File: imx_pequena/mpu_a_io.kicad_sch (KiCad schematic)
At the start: 23 parts, among them J1 Conn_ARM_JTAG_SWD_10, U1 MCIMX6Z0DVM09AB, Y1 Crystal, Y2 Crystal

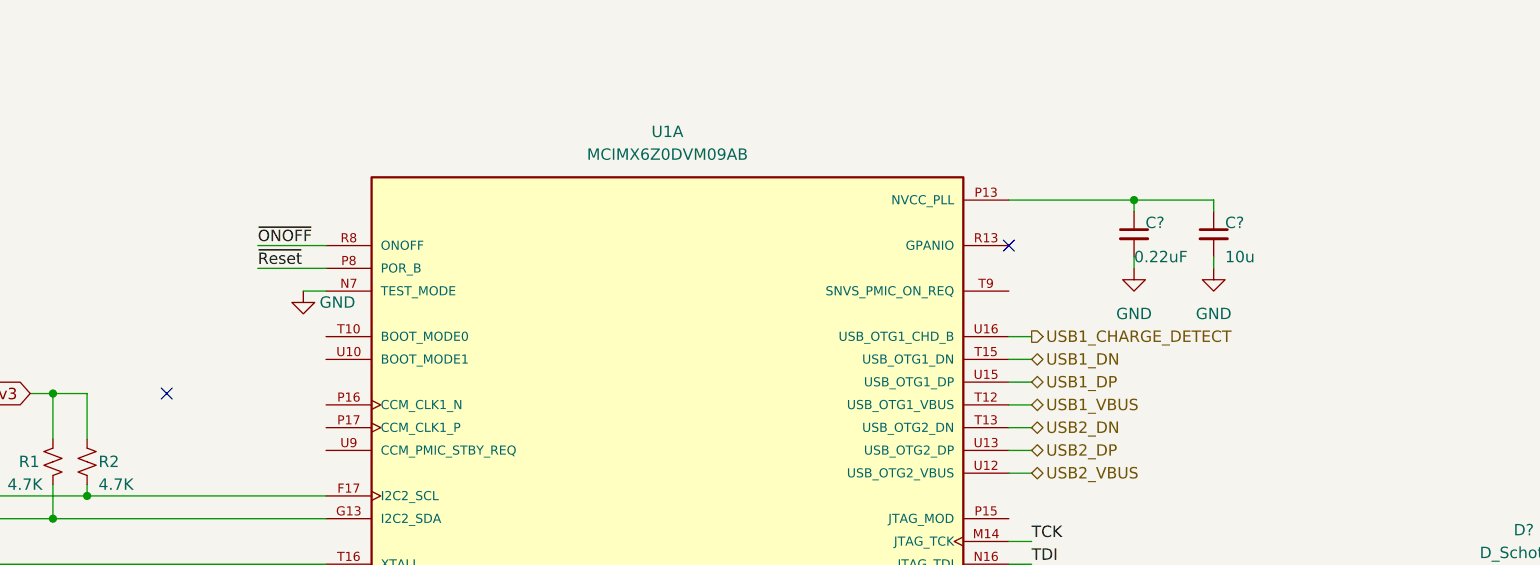
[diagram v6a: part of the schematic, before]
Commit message: Cleaned up NVCC pins
Added 3v3 connections + decoupling caps to NVcc pins
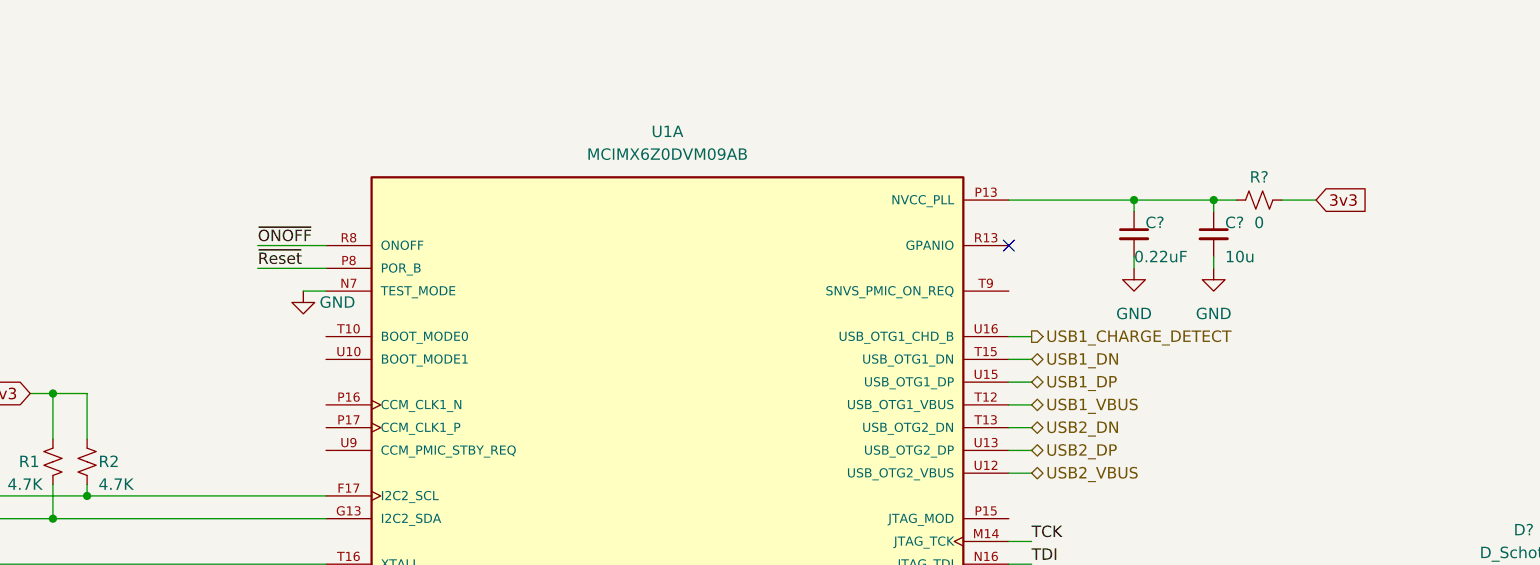
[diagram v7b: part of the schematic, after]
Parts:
- added R?: 0, symbol Device:R_Small_US
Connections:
- net at C?.1, C?.1, U1.P13 (NVCC_PLL): now also R?.1
- new net 3v3: R?.2
- no-connect marks 2 -> 1
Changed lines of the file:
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@@
   (junction (at 199.39 58.42) (diameter 0) (color 0 0 0 0)
   )
+  (junction (at 208.28 58.42) (diameter 0) (color 0 0 0 0)
+  )
   (junction (at 29.21 36.83) (diameter 0) (color 0 0 0 0)
   )
@@
   )
   (no_connect (at 185.42 63.5))
-  (no_connect (at 91.44 80.01))
   (wire (pts (xy 199.39 58.42) (xy 199.39 59.69))
     (stroke (width 0) (type default) (color 0 0 0 0))
@@
     (stroke (width 0) (type default) (color 0 0 0 0))
   )
+  (wire (pts (xy 208.28 58.42) (xy 210.82 58.42))
+    (stroke (width 0) (type default) (color 0 0 0 0))
+  )
   (wire (pts (xy 247.65 17.78) (xy 247.65 20.32))
     (stroke (width 0) (type default) (color 0 0 0 0))
@@
   )
   (wire (pts (xy 59.69 22.86) (xy 57.15 22.86))
+    (stroke (width 0) (type default) (color 0 0 0 0))
+  )
+  (wire (pts (xy 215.9 58.42) (xy 219.71 58.42))
     (stroke (width 0) (type default) (color 0 0 0 0))
   )
@@
     (property "Intersheet References" "${INTERSHEET_REFS}" (id 0) (at 45.3026 22.7806 0)
       (effects (font (size 1.27 1.27)) (justify right) hide)
+    )
+  )
+  (global_label "3v3" (shape input) (at 219.71 58.42 0) (fields_autoplaced)
+    (effects (font (size 1.27 1.27)) (justify left))
+    (property "Intersheet References" "${INTERSHEET_REFS}" (id 0) (at 225.5098 58.3406 0)
+      (effects (font (size 1.27 1.27)) (justify left) hide)
     )
   )
@@
       (effects (font (size 1.27 1.27)) hide)
     )
+    (pin "1")
+    (pin "2")
+  )
+  (symbol (lib_id "Device:R_Small_US") (at 213.36 58.42 90) (unit 1)
+    (in_bom yes) (on_board yes)
+    (property "Reference" "R?" (id 0) (at 213.36 55.88 90))
+    (property "Value" "0" (id 1) (at 213.36 60.96 90))
+    (property "Footprint" "" (id 2) (at 213.36 58.42 0)
+      (effects (font (size 1.27 1.27)) hide)
+    )
+    (property "Datasheet" "~" (id 3) (at 213.36 58.42 0)
+      (effects (font (size 1.27 1.27)) hide)
+    )

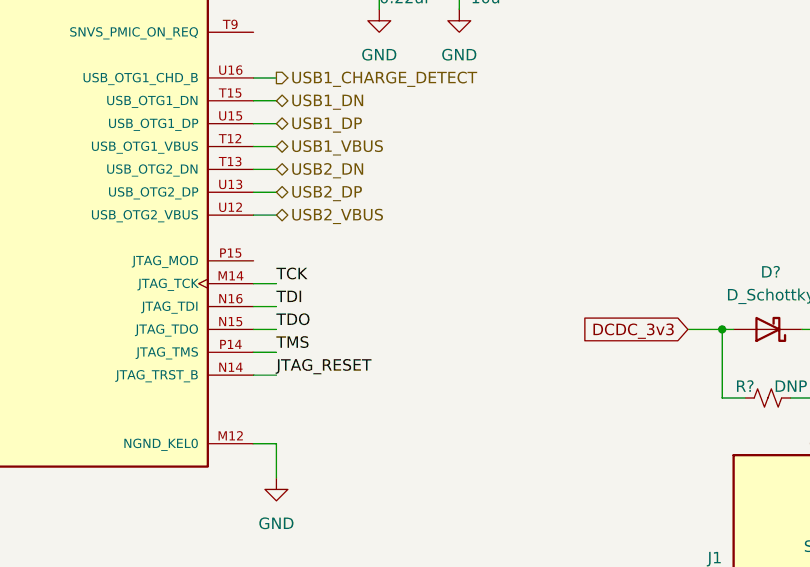
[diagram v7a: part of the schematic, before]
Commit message: Updated pin mappings
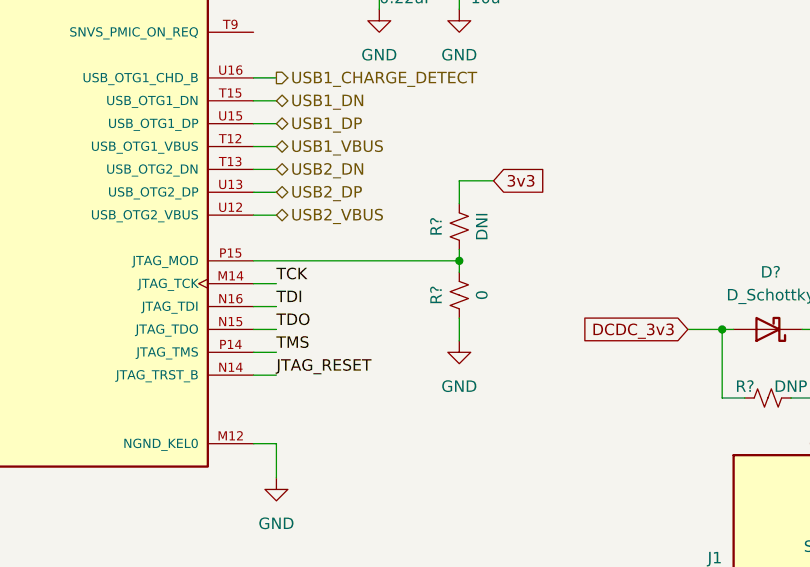
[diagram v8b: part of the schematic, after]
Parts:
- added R?: 0, symbol Device:R_Small_US
- added R?: DNI, symbol Device:R_Small_US
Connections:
- net 3v3: now also R?.2
- net GND: now also R?.1
- net at U1.P15 (JTAG_MOD): now also R?.1, R?.2
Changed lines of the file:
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@@
   (junction (at 208.28 58.42) (diameter 0) (color 0 0 0 0)
+  )
+  (junction (at 208.28 93.98) (diameter 0) (color 0 0 0 0)
   )
   (junction (at 29.21 36.83) (diameter 0) (color 0 0 0 0)
@@
     (stroke (width 0) (type default) (color 0 0 0 0))
   )
+  (wire (pts (xy 208.28 85.09) (xy 212.09 85.09))
+    (stroke (width 0) (type default) (color 0 0 0 0))
+  )
   (wire (pts (xy 185.42 101.6) (xy 187.96 101.6))
     (stroke (width 0) (type default) (color 0 0 0 0))
@@
     (stroke (width 0) (type default) (color 0 0 0 0))
   )
+  (wire (pts (xy 208.28 92.71) (xy 208.28 93.98))
+    (stroke (width 0) (type default) (color 0 0 0 0))
+  )
   (wire (pts (xy 102.87 114.3) (xy 104.14 114.3))
     (stroke (width 0) (type default) (color 0 0 0 0))
@@
     (stroke (width 0) (type default) (color 0 0 0 0))
   )
+  (wire (pts (xy 208.28 93.98) (xy 208.28 95.25))
+    (stroke (width 0) (type default) (color 0 0 0 0))
+  )
   (wire (pts (xy 185.42 104.14) (xy 187.96 104.14))
     (stroke (width 0) (type default) (color 0 0 0 0))
@@
     (stroke (width 0) (type default) (color 0 0 0 0))
   )
+  (wire (pts (xy 185.42 93.98) (xy 208.28 93.98))
+    (stroke (width 0) (type default) (color 0 0 0 0))
+  )
   (wire (pts (xy 246.38 144.78) (xy 246.38 143.51))
     (stroke (width 0) (type default) (color 0 0 0 0))
@@
     (stroke (width 0) (type default) (color 0 0 0 0))
   )
+  (wire (pts (xy 208.28 100.33) (xy 208.28 102.87))
+    (stroke (width 0) (type default) (color 0 0 0 0))
+  )
   (wire (pts (xy 66.04 93.98) (xy 78.74 93.98))
     (stroke (width 0) (type default) (color 0 0 0 0))
@@
   )
   (wire (pts (xy 82.55 85.09) (xy 82.55 80.01))
+    (stroke (width 0) (type default) (color 0 0 0 0))
+  )
+  (wire (pts (xy 208.28 87.63) (xy 208.28 85.09))
     (stroke (width 0) (type default) (color 0 0 0 0))
   )
@@
     (effects (font (size 1.27 1.27)) (justify left))
     (property "Intersheet References" "${INTERSHEET_REFS}" (id 0) (at 225.5098 58.3406 0)
+      (effects (font (size 1.27 1.27)) (justify left) hide)
+    )
+  )
+  (global_label "3v3" (shape input) (at 212.09 85.09 0) (fields_autoplaced)
+    (effects (font (size 1.27 1.27)) (justify left))
+    (property "Intersheet References" "${INTERSHEET_REFS}" (id 0) (at 217.8898 85.0106 0)
       (effects (font (size 1.27 1.27)) (justify left) hide)
     )
@@
     (pin "1")
   )
+  (symbol (lib_id "power:GND") (at 208.28 102.87 0) (unit 1)
+    (in_bom yes) (on_board yes) (fields_autoplaced)
+    (property "Reference" "#PWR?" (id 0) (at 208.28 109.22 0)
+      (effects (font (size 1.27 1.27)) hide)
+    )
+    (property "Value" "GND" (id 1) (at 208.28 107.95 0))
+    (property "Footprint" "" (id 2) (at 208.28 102.87 0)
+      (effects (font (size 1.27 1.27)) hide)
+    )
+    (property "Datasheet" "" (id 3) (at 208.28 102.87 0)
+      (effects (font (size 1.27 1.27)) hide)
+    )
+    (pin "1")
+  )
   (symbol (lib_id "power:GND") (at 247.65 30.48 0) (unit 1)
     (in_bom yes) (on_board yes) (fields_autoplaced)
@@
     (pin "2")
   )
+  (symbol (lib_id "Device:R_Small_US") (at 208.28 97.79 180) (unit 1)
+    (in_bom yes) (on_board yes)
+    (property "Reference" "R?" (id 0) (at 205.74 97.79 90))
+    (property "Value" "0" (id 1) (at 210.82 97.79 90))
+    (property "Footprint" "" (id 2) (at 208.28 97.79 0)
+      (effects (font (size 1.27 1.27)) hide)
+    )
+    (property "Datasheet" "~" (id 3) (at 208.28 97.79 0)
+      (effects (font (size 1.27 1.27)) hide)
+    )
+    (pin "1")
+    (pin "2")
+  )
   (symbol (lib_id "power:GND") (at 187.96 118.11 0) (unit 1)
     (in_bom yes) (on_board yes) (fields_autoplaced)
@@
     (pin "1")
   )
+  (symbol (lib_id "Device:R_Small_US") (at 208.28 90.17 180) (unit 1)
+    (in_bom yes) (on_board yes)
+    (property "Reference" "R?" (id 0) (at 205.74 90.17 90))
+    (property "Value" "DNI" (id 1) (at 210.82 90.17 90))
+    (property "Footprint" "" (id 2) (at 208.28 90.17 0)
+      (effects (font (size 1.27 1.27)) hide)
+    )
+    (property "Datasheet" "~" (id 3) (at 208.28 90.17 0)
+      (effects (font (size 1.27 1.27)) hide)
+    )
+    (pin "1")
+    (pin "2")
+  )
   (symbol (lib_id "Device:R_Small_US") (at 59.69 30.48 0) (unit 1)
